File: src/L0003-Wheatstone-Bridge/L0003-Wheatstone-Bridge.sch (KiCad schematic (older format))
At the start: 18 parts, among them P1 12V, P2 2043-1X04G00DAU, U1 MCP1703T-4002E_DB

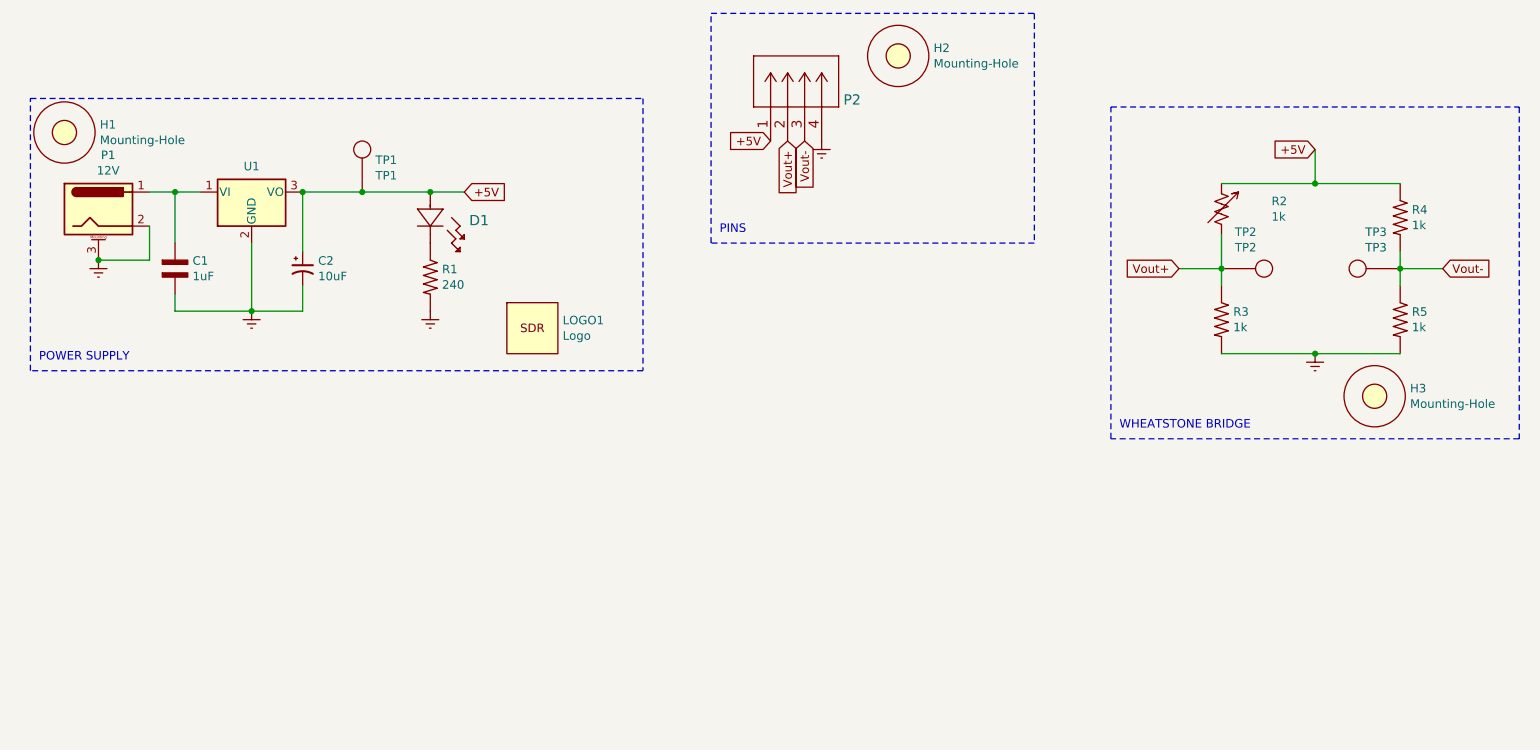
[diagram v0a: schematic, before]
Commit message: Made circuit look nicer (MISC box & TP points)
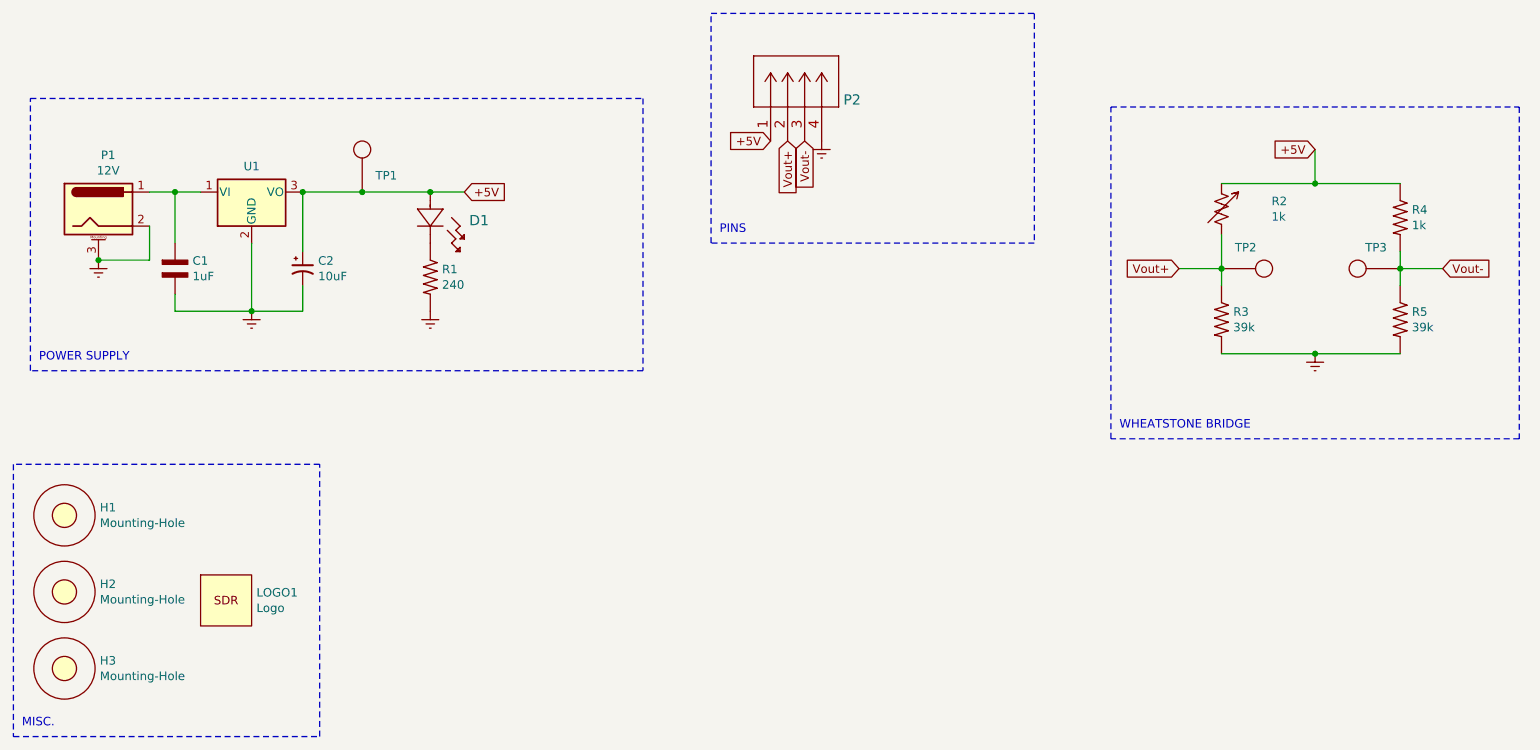
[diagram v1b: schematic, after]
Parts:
- R3, R5: value 1k -> 39k
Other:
- note added: "MISC."
- moved on the sheet: H1, H2, H3, LOGO1
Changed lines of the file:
@@
 U 1 1 617603D5
 P 2750 2550
-F 0 "TP1" H 2828 2738 50  0000 L CNN
+F 0 "TP1" H 2828 2738 50  0001 L CNN
 F 1 "TP1" H 2828 2647 50  0000 L CNN
 F 2 "" H 2750 2550 50  0001 C CNN
@@
 U 1 1 6177A074
 P 7800 3000
-F 0 "TP2" V 7585 3142 50  0000 C CNN
+F 0 "TP2" V 7585 3142 50  0001 C CNN
 F 1 "TP2" V 7676 3142 50  0000 C CNN
 F 2 "" H 7800 3000 50  0001 C CNN
@@
 U 1 1 6177A6FC
 P 8850 3000
-F 0 "TP3" V 9065 3142 50  0000 C CNN
+F 0 "TP3" V 9065 3142 50  0001 C CNN
 F 1 "TP3" V 8974 3142 50  0000 C CNN
 F 2 "" H 8850 3000 50  0001 C CNN
@@
 P 7800 3300
 F 0 "R3" V 7754 3369 50  0000 L CNN
-F 1 "1k" V 7845 3369 50  0000 L CNN
+F 1 "39k" V 7845 3369 50  0000 L CNN
 F 2 "" H 7850 2800 50  0001 L BNN
 F 3 "" H 7800 3300 50  0001 L BNN
@@
 P 8850 3300
 F 0 "R5" V 8804 3369 50  0000 L CNN
-F 1 "1k" V 8895 3369 50  0000 L CNN
+F 1 "39k" V 8895 3369 50  0000 L CNN
 F 2 "" H 8900 2800 50  0001 L BNN
 F 3 "" H 8850 3300 50  0001 L BNN
@@
 L L0003-Wheatstone-Bridge:Mounting-Hole H1
 U 1 1 61793FCB
-P 1000 2200
-F 0 "H1" H 1208 2246 50  0000 L CNN
-F 1 "Mounting-Hole" H 1208 2155 50  0000 L CNN
-F 2 "" H 1000 2200 50  0001 C CNN
-F 3 "" H 1000 2200 50  0001 C CNN
-	1    1000 2200
+P 1000 4450
+F 0 "H1" H 1208 4496 50  0000 L CNN
+F 1 "Mounting-Hole" H 1208 4405 50  0000 L CNN
+F 2 "" H 1000 4450 50  0001 C CNN
+F 3 "" H 1000 4450 50  0001 C CNN
+	1    1000 4450
 	1    0    0    -1
 $EndComp
@@
 L L0003-Wheatstone-Bridge:Mounting-Hole H2
 U 1 1 617947D8
-P 5900 1750
-F 0 "H2" H 6108 1796 50  0000 L CNN
-F 1 "Mounting-Hole" H 6108 1705 50  0000 L CNN
-F 2 "" H 5900 1750 50  0001 C CNN
-F 3 "" H 5900 1750 50  0001 C CNN
-	1    5900 1750
-	1    0    0    -1
-$EndComp
-$Comp
-L L0003-Wheatstone-Bridge:Mounting-Hole H3
-U 1 1 617992D5
-P 8700 3750
-F 0 "H3" H 8908 3796 50  0000 L CNN
-F 1 "Mounting-Hole" H 8908 3705 50  0000 L CNN
-F 2 "" H 8700 3750 50  0001 C CNN
-F 3 "" H 8700 3750 50  0001 C CNN
-	1    8700 3750
+P 1000 4900
+F 0 "H2" H 1208 4946 50  0000 L CNN
+F 1 "Mounting-Hole" H 1208 4855 50  0000 L CNN
+F 2 "" H 1000 4900 50  0001 C CNN
+F 3 "" H 1000 4900 50  0001 C CNN
+	1    1000 4900
 	1    0    0    -1
 $EndComp
@@
 Wire Notes Line
 	4800 2850 4800 1500
-$Comp
-L L0003-Wheatstone-Bridge:Logo LOGO1
-U 1 1 6179FC65
-P 3750 3350
-F 0 "LOGO1" H 3928 3396 50  0000 L CNN
-F 1 "Logo" H 3928 3305 50  0000 L CNN
-F 2 "" H 3750 3350 50  0001 C CNN
-F 3 "" H 3750 3350 50  0001 C CNN
-	1    3750 3350
-	1    0    0    -1
-$EndComp
 Connection ~ 8350 2500
 Wire Wire Line
@@
 Wire Wire Line
 	8850 3000 9100 3000
+Wire Notes Line
+	700  4150 700  5750
+Wire Notes Line
+	700  5750 2500 5750
+Wire Notes Line
+	2500 5750 2500 4150
+Wire Notes Line
+	2500 4150 700  4150
+Text Notes 750  5700 0    50   ~ 0
+MISC.
+$Comp
+L L0003-Wheatstone-Bridge:Mounting-Hole H3
+U 1 1 617992D5
+P 1000 5350
+F 0 "H3" H 1208 5396 50  0000 L CNN
+F 1 "Mounting-Hole" H 1208 5305 50  0000 L CNN
+F 2 "" H 1000 5350 50  0001 C CNN
+F 3 "" H 1000 5350 50  0001 C CNN
+	1    1000 5350
+	1    0    0    -1
+$EndComp
+$Comp
+L L0003-Wheatstone-Bridge:Logo LOGO1
+U 1 1 6179FC65
+P 1950 4950
+F 0 "LOGO1" H 2128 4996 50  0000 L CNN
+F 1 "Logo" H 2128 4905 50  0000 L CNN
+F 2 "" H 1950 4950 50  0001 C CNN
+F 3 "" H 1950 4950 50  0001 C CNN
+	1    1950 4950
+	1    0    0    -1
+$EndComp
 $EndSCHEMATC

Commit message: Created PCB Layout
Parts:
- C1: footprint (none) -> L0003-Wheatstone-Bridge:CAP_0603
- C2: footprint (none) -> L0003-Wheatstone-Bridge:T491A106K010AT
- D1: footprint (none) -> L0003-Wheatstone-Bridge:SML-LX1206GC-TR
- H1, H2, H3: footprint (none) -> L0003-Wheatstone-Bridge:MountingHole_2.1mm
- LOGO1: footprint (none) -> L0003-Wheatstone-Bridge:logo2
- P1: footprint (none) -> L0003-Wheatstone-Bridge:12V_power_jack
- P2: footprint CONN_2043-1X04G00DAU_OUP -> L0003-Wheatstone-Bridge:SULLINS_PPTC041LFBN-RC
- R1, R3, R4, R5: footprint (none) -> L0003-Wheatstone-Bridge:RES_0603
- R2: footprint (none) -> L0003-Wheatstone-Bridge:TRIM_3310Y-001-102L
- TP1, TP2, TP3: footprint (none) -> L0003-Wheatstone-Bridge:TP
- U1: footprint Package_TO_SOT_SMD:SOT-223-3_TabPin2 -> L0003-Wheatstone-Bridge:MCP1703T-4002E&slash_DB
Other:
- moved on the sheet: H1, H2, H3, LOGO1, P2, R2, R3, R4, R5

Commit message: Finished PCB
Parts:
- U1: footprint L0003-Wheatstone-Bridge:MCP1703T-4002E&slash_DB -> Package_TO_SOT_SMD:SOT-223-3_TabPin2
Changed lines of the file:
@@
 F 0 "U1" H 2100 2701 50  0000 C CNN
 F 1 "MCP1703T-4002E_DB" H 2100 2675 50  0001 L CNN
-F 2 "L0003-Wheatstone-Bridge:MCP1703T-4002E&slash_DB" H 2100 2750 50  0001 C CNN
+F 2 "Package_TO_SOT_SMD:SOT-223-3_TabPin2" H 2100 2750 50  0001 C CNN
 F 3 "" H 2100 2500 50  0001 C CNN
 	1    2100 2550

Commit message: Changed Wire connecting power to VRM
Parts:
- U1: footprint Package_TO_SOT_SMD:SOT-223-3_TabPin2 -> L0003-Wheatstone-Bridge:MCP1703T-4002E&slash_DB
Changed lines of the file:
@@
 F 0 "U1" H 2100 2701 50  0000 C CNN
 F 1 "MCP1703T-4002E_DB" H 2100 2675 50  0001 L CNN
-F 2 "Package_TO_SOT_SMD:SOT-223-3_TabPin2" H 2100 2750 50  0001 C CNN
+F 2 "L0003-Wheatstone-Bridge:MCP1703T-4002E&slash_DB" H 2100 2750 50  0001 C CNN
 F 3 "" H 2100 2500 50  0001 C CNN
 	1    2100 2550
